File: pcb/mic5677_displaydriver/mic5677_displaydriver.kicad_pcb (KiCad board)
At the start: 2 copper layers, 180 x 110 mm, 81 parts, among them J1 Segment DIP14, J2 Segment DIP14, J3 Segment Wire Connector, J4 Common Cathode Enable, J5 PSU, J6 Bypass, J7 Serial Debug, J8 8P8C, Q1 D45H8G, Q10 BC546, Q11 BC546, Q12 BC546, Q13 BC546, Q14 BC546, Q15 BC546, Q16 BC546, Q17 BC546, Q18 BC546, Q19 BC546, Q2 D45H8G, Q20 BC546, Q21 BC546, Q22 BC546, Q23 BC546, Q3 D45H8G, Q4 D45H8G, Q5 D45H8G, Q6 D45H8G, Q7 D45H8G, Q8 D45H8G, Q9 D45H8G, U1 L7805, U2 74HC595, U3 74HC595, U4 74HC02

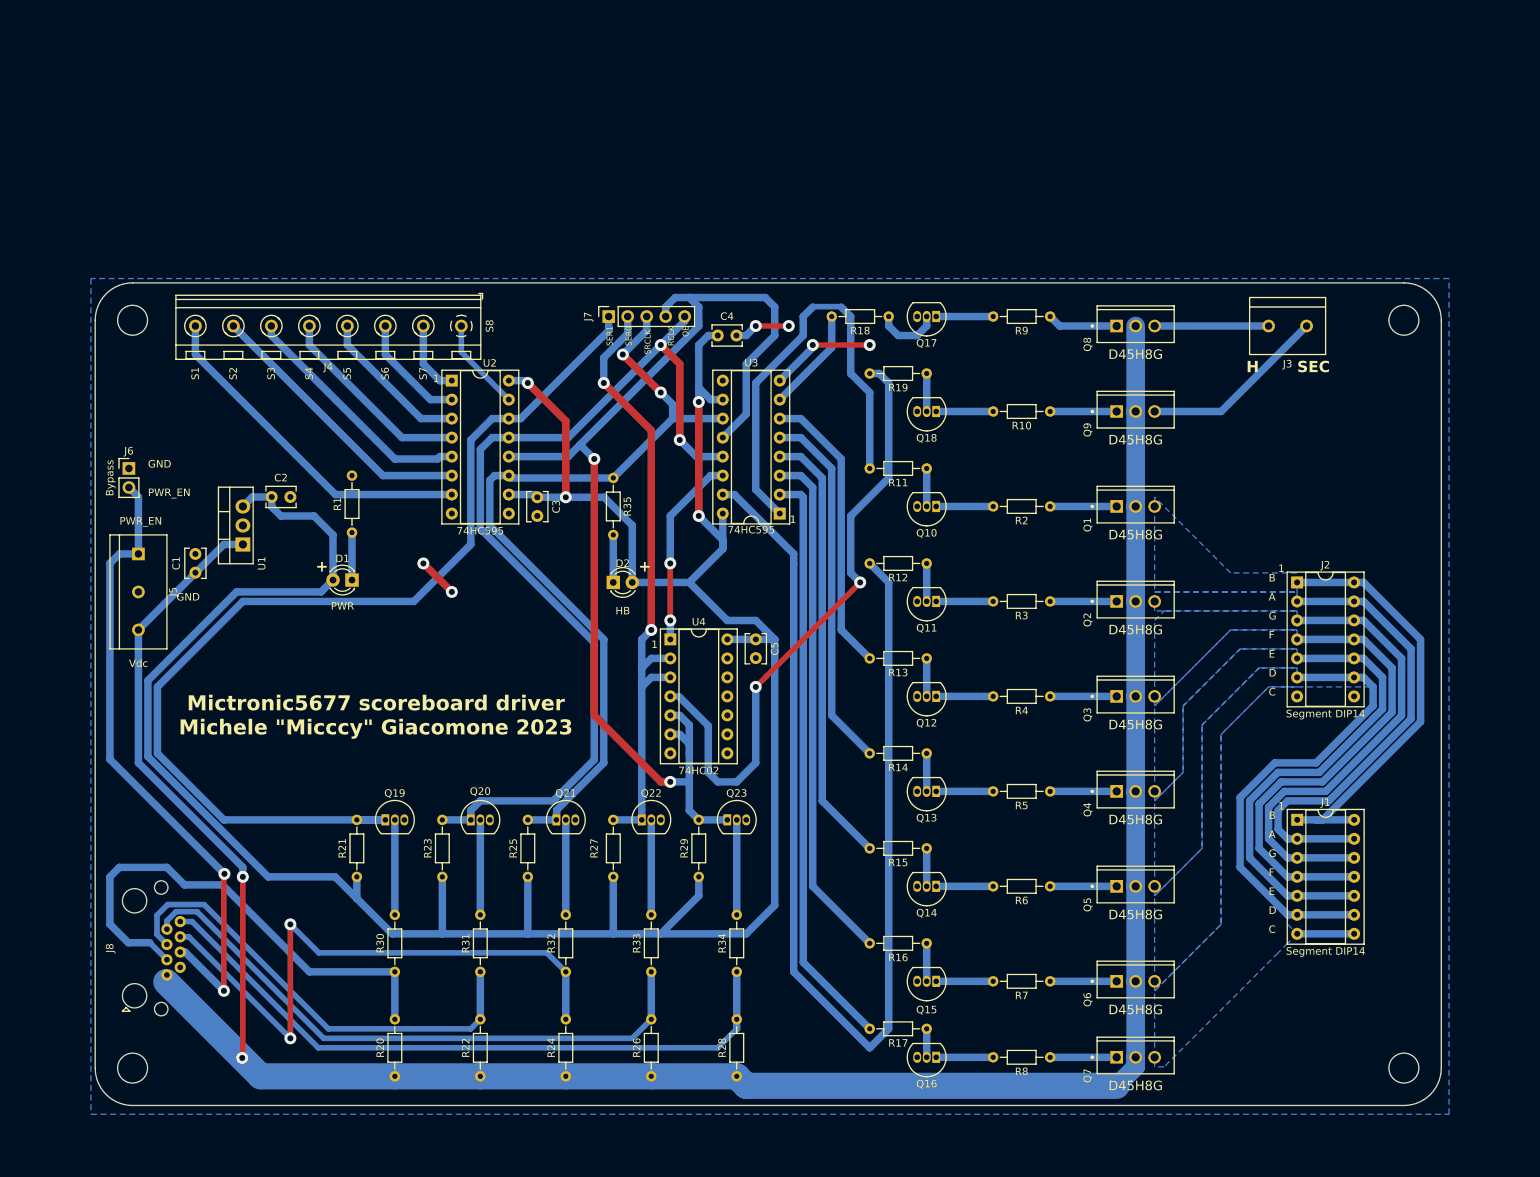
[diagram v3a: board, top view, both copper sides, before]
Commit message: Made display driver pcb slightly worse but easier to manufacture
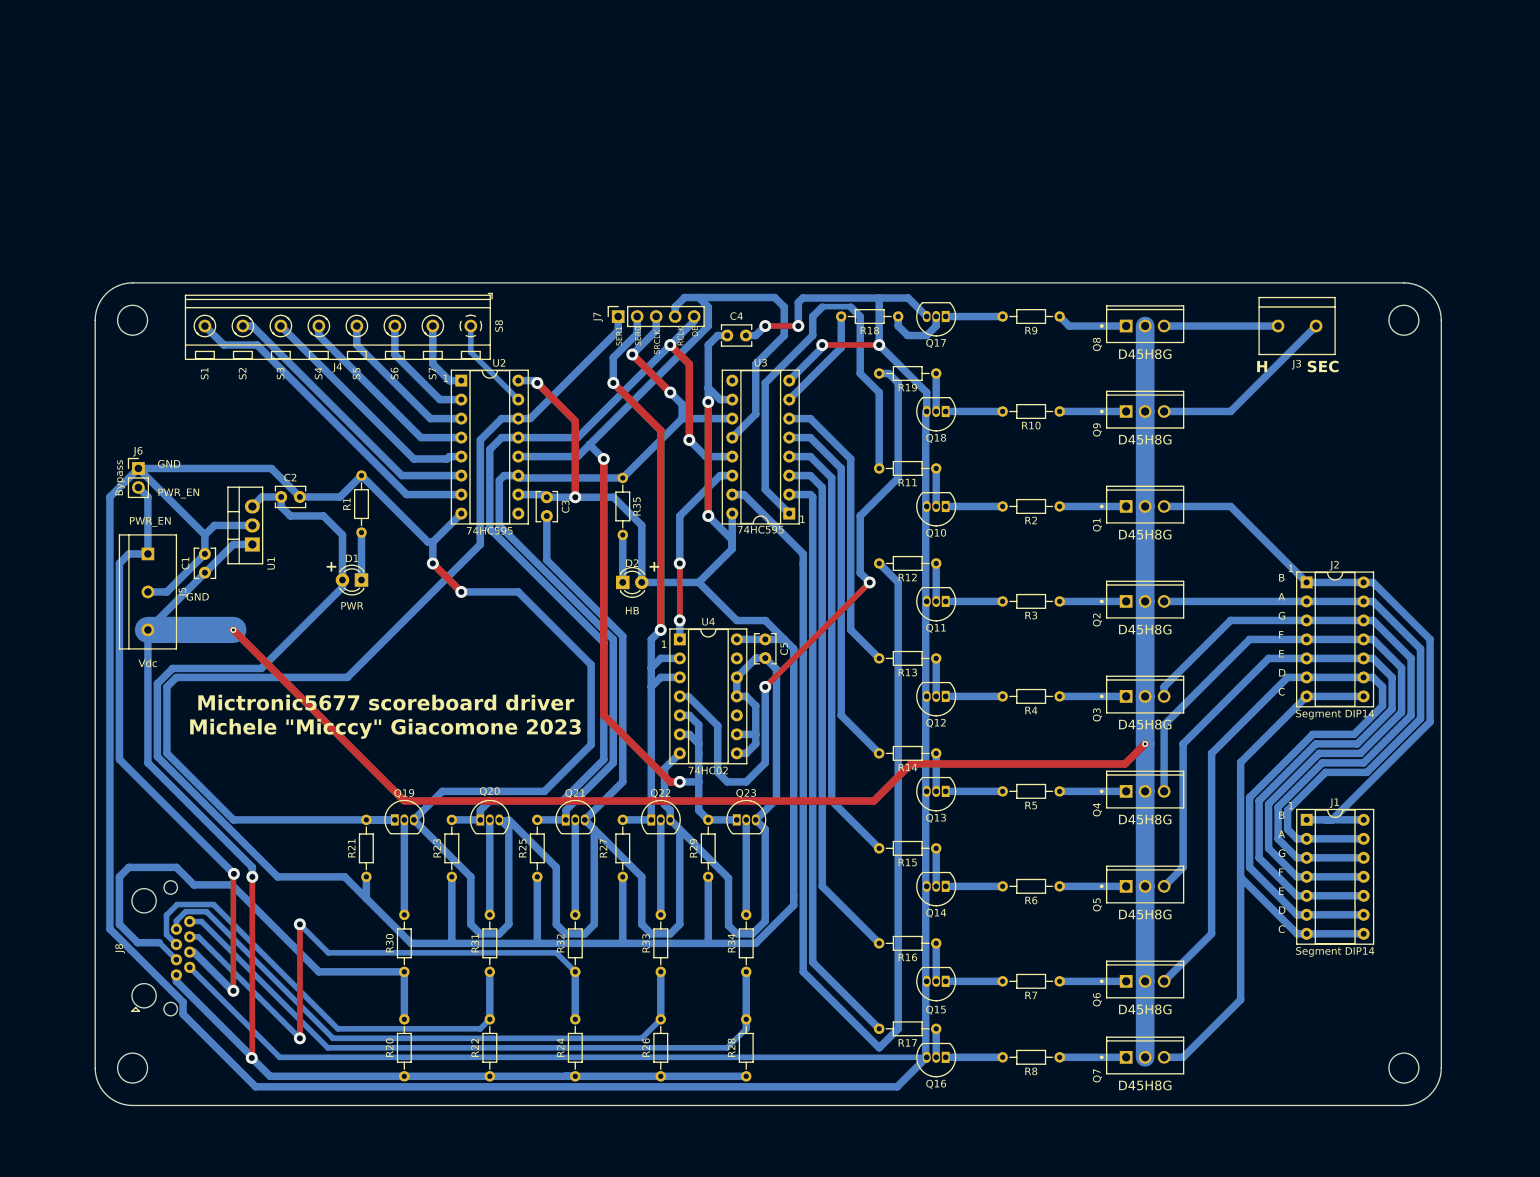
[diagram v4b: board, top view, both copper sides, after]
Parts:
- moved C2 1.27 mm to (69.9, 73.6)
- moved C4 1.27 mm to (129.5, 52.0)
- moved C5 1.27 mm to (134.6, 92.7)
- moved J1 1.27 mm to (207.0, 116.8)
- moved J2 1.27 mm to (207.0, 85.1)
- moved J4 1.27 mm to (95.2, 50.8)
- moved Q1 1.27 mm to (185.4, 74.9)
- moved Q2 1.27 mm to (185.4, 87.6)
- moved Q21 1.27 mm to (107.9, 116.8)
- moved Q3 1.27 mm to (185.4, 100.3)
- moved Q4 1.27 mm to (185.4, 113.0)
- moved Q5 1.27 mm to (185.4, 125.7)
- moved Q6 1.27 mm to (185.4, 138.4)
- moved Q7 1.27 mm to (185.4, 148.6)
- moved Q8 1.27 mm to (185.4, 50.8)
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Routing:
- net GND: track 26.7 -> 839.3 mm
- net VDC: track 317.2 -> 409.2 mm, vias 2 -> 4
- net /C_OUT: track 7.62 -> 84.9 mm
- net /D_OUT: track 63.3 -> 113.3 mm
- net /E_OUT: track 63.3 -> 104.6 mm
- net /F_OUT: track 63.3 -> 96.0 mm
- net /G_OUT: track 63.3 -> 87.3 mm
- net /B_OUT: track 57.7 -> 81.0 mm
- net /A_OUT: track 63.3 -> 82.3 mm
- net +5V: track 349.3 -> 355.4 mm
- net /S1: track 45.9 -> 43.6 mm
- net /S3: track 32.4 -> 31.6 mm
- net /S4: track 26.7 -> 26.0 mm
- removed copper zone on B.Cu, net /A_OUT
- removed copper zone on B.Cu, net /B_OUT
- removed copper zone on B.Cu, net /C_OUT
- removed copper zone on B.Cu, net /D_OUT
- removed copper zone on B.Cu, net /E_OUT
- removed copper zone on B.Cu, net /F_OUT
- removed copper zone on B.Cu, net /G_OUT
- removed copper zone on B.Cu, net GND

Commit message: Added back fill zones to display driver pcb
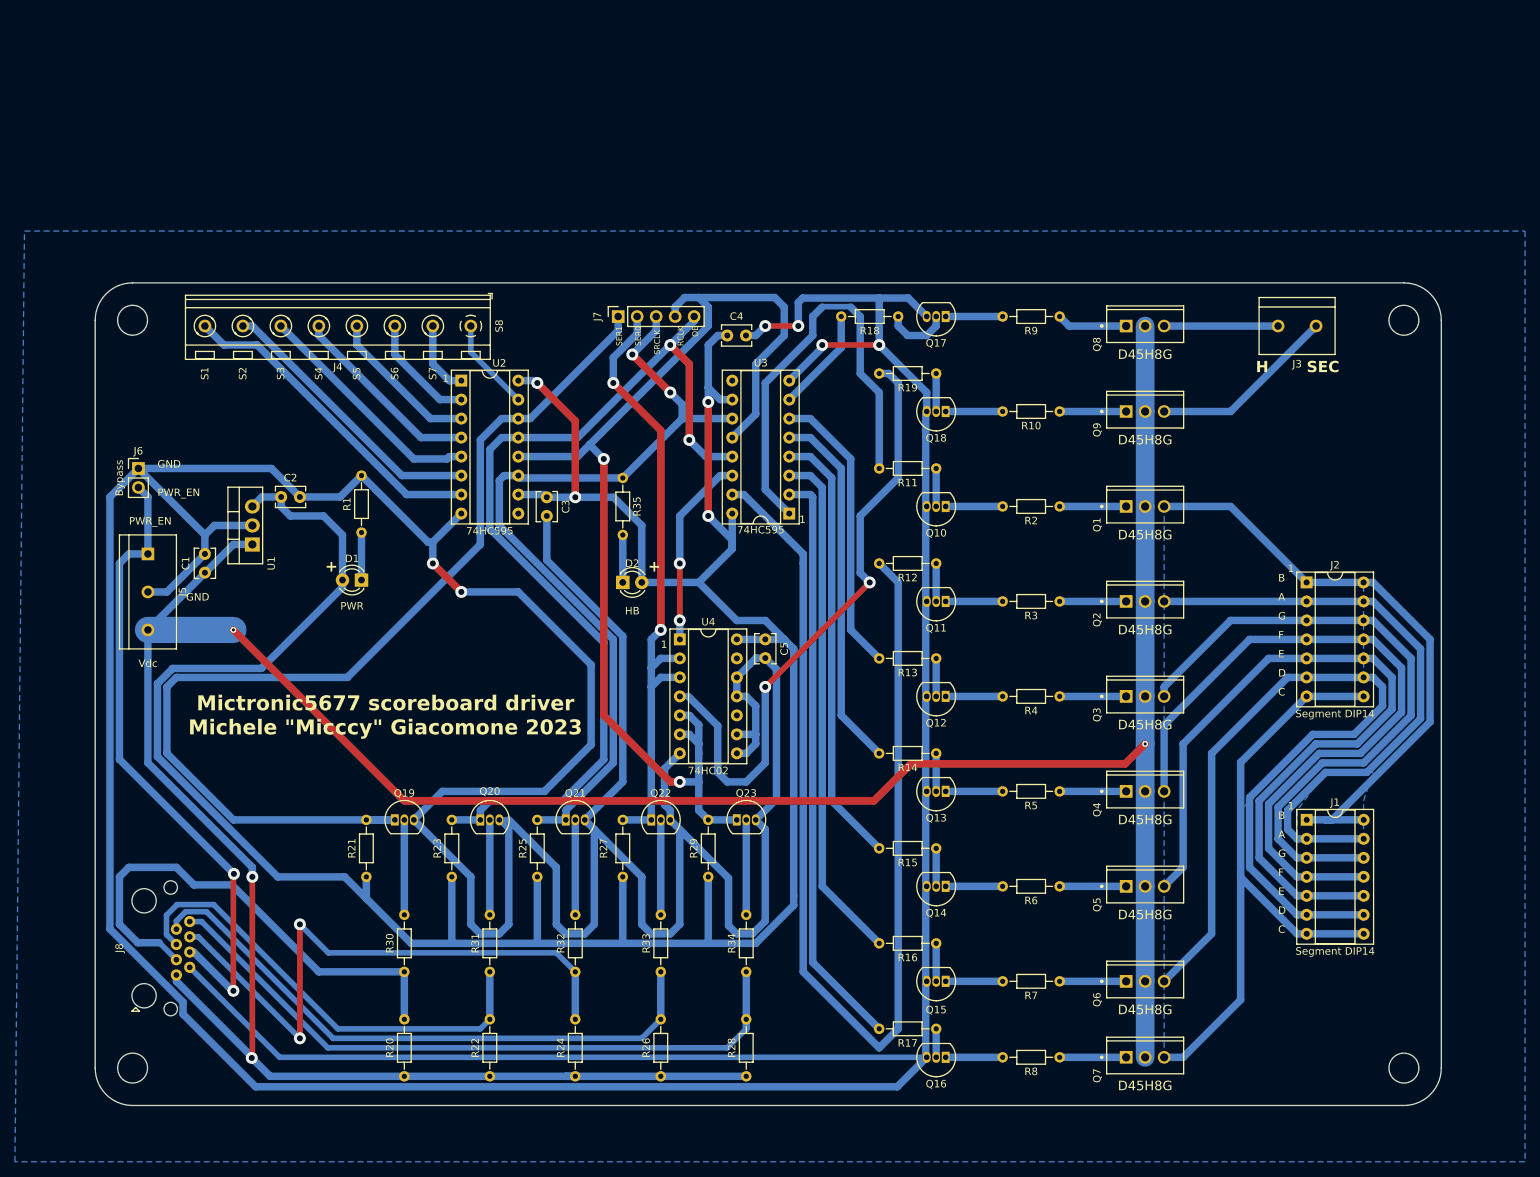
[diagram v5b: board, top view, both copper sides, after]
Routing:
- added copper zone on B.Cu, net /B_OUT
- added copper zone on B.Cu, net /C_OUT
- added copper zone on B.Cu, net /D_OUT
- added copper zone on B.Cu, net /E_OUT
- added copper zone on B.Cu, net /F_OUT
- added copper zone on B.Cu, net /G_OUT
- added copper zone on B.Cu, net GND
